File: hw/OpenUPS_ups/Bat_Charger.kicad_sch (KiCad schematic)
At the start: 63 parts, among them Q406 PMOS, Q601 2N7002, Q701 AON7534, U402 BD99950, U403 MCP6001R, U404 DZDH0401DW, U405 INA180A1, U801 NCP431

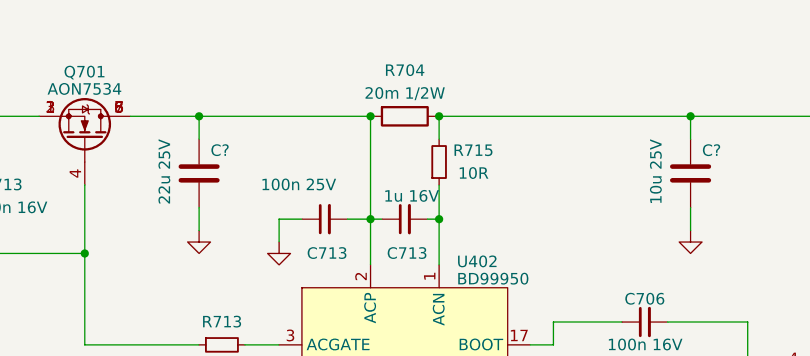
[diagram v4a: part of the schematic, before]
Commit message: Unified sense resistors to 10mR; Placement
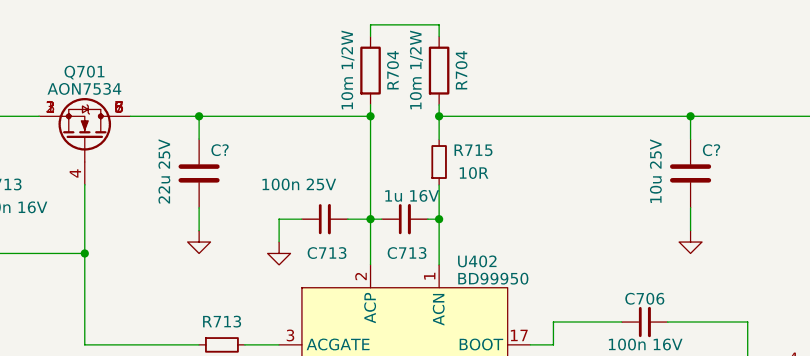
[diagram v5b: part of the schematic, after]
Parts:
- removed R704: 20m 1/2W, Resistor_SMD:R_2512_6332Metric, symbol Device:R
- added R704 (x2): 10m 1/2W, Resistor_SMD:R_1206_3216Metric, symbol Device:R
- R704: footprint Resistor_SMD:R_2512_6332Metric -> Resistor_SMD:R_1206_3216Metric
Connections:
- net at C?.1, Q701.5 (D), Q701.6 (D)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: now also R704.2
- net at C713.1, C713.2, C?.1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: now also R704.2
- new net: R704.1, R704.1
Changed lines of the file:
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@@
   (junction (at 186.69 78.74) (diameter 0) (color 0 0 0 0)
   )
-  (junction (at 161.29 25.4) (diameter 0) (color 0 0 0 0)
+  (junction (at 125.73 25.4) (diameter 0) (color 0 0 0 0)
   )
-  (junction (at 133.35 25.4) (diameter 0) (color 0 0 0 0)
+  (junction (at 161.29 25.4) (diameter 0) (color 0 0 0 0)
   )
   (junction (at 351.79 60.96) (diameter 0) (color 0 0 0 0)
@@
   (junction (at 245.11 69.85) (diameter 0) (color 0 0 0 0)
   )
-  (junction (at 125.73 25.4) (diameter 0) (color 0 0 0 0)
-  )
   (junction (at 133.35 36.83) (diameter 0) (color 0 0 0 0)
   )
@@
   (junction (at 240.03 217.17) (diameter 0) (color 0 0 0 0)
   )
+  (junction (at 133.35 25.4) (diameter 0) (color 0 0 0 0)
+  )
   (junction (at 368.3 102.87) (diameter 0) (color 0 0 0 0)
   )
@@
     (stroke (width 0) (type default))
   )
+  (wire (pts (xy 125.73 15.24) (xy 133.35 15.24))
+    (stroke (width 0) (type default))
+  )
   (wire (pts (xy 72.39 49.53) (xy 78.74 49.53))
     (stroke (width 0) (type default))
@@
     (stroke (width 0) (type default))
   )
-  (wire (pts (xy 133.35 25.4) (xy 161.29 25.4))
-    (stroke (width 0) (type default))
-  )
   (wire (pts (xy 80.01 36.83) (xy 80.01 40.64))
     (stroke (width 0) (type default))
@@
     (stroke (width 0) (type default))
   )
+  (wire (pts (xy 125.73 16.51) (xy 125.73 15.24))
+    (stroke (width 0) (type default))
+  )
   (wire (pts (xy 106.68 25.4) (xy 125.73 25.4))
     (stroke (width 0) (type default))
@@
     (stroke (width 0) (type default))
   )
+  (wire (pts (xy 133.35 25.4) (xy 133.35 24.13))
+    (stroke (width 0) (type default))
+  )
   (wire (pts (xy 106.68 38.1) (xy 106.68 35.56))
     (stroke (width 0) (type default))
@@
     (stroke (width 0) (type default))
   )
+  (wire (pts (xy 133.35 25.4) (xy 161.29 25.4))
+    (stroke (width 0) (type default))
+  )
   (wire (pts (xy 361.95 60.96) (xy 375.92 60.96))
     (stroke (width 0) (type default))
@@
     (stroke (width 0) (type default))
   )
+  (wire (pts (xy 125.73 24.13) (xy 125.73 25.4))
+    (stroke (width 0) (type default))
+  )
   (wire (pts (xy 361.95 73.66) (xy 361.95 71.12))
     (stroke (width 0) (type default))
@@
     (stroke (width 0) (type default))
   )
+  (wire (pts (xy 133.35 15.24) (xy 133.35 16.51))
+    (stroke (width 0) (type default))
+  )
   (wire (pts (xy 198.12 66.04) (xy 198.12 67.31))
     (stroke (width 0) (type default))
@@
     )
   )
+  (symbol (lib_id "Device:R") (at 125.73 20.32 0) (unit 1)
+    (in_bom yes) (on_board yes) (dnp no)
+    (property "Reference" "R704" (at 128.27 20.32 90)
+      (effects (font (size 1.27 1.27)))
+    )
+    (property "Value" "10m 1/2W" (at 123.19 20.32 90)
+      (effects (font (size 1.27 1.27)))
+    )
+    (property "Footprint" "Resistor_SMD:R_1206_3216Metric" (at 123.952 20.32 90)
+      (effects (font (size 1.27 1.27)) hide)
+    )
+    (property "Datasheet" "~" (at 125.73 20.32 0)
+      (effects (font (size 1.27 1.27)) hide)
+    )
+    (pin "1")
+    (pin "2")
+    (instances
+      (project "OpenUPS_ups"
+        (path "/f77faec3-eac4-47f3-a2de-ec4a039f4502/09fcd86a-cc7e-4bce-97cb-42a94055ba63"
+          (reference "R704") (unit 1)
+        )
+        (path "/f77faec3-eac4-47f3-a2de-ec4a039f4502/dfbaaed0-e564-4e21-900d-d5a65c0f1694"
+          (reference "R410") (unit 1)
+        )
+        (path "/f77faec3-eac4-47f3-a2de-ec4a039f4502/0bd99307-a15c-41e8-997b-077d576f806c"
+          (reference "R424") (unit 1)
+        )
+      )
+    )
+  )
   (symbol (lib_id "power:GND") (at 281.94 77.47 90) (unit 1)
     (in_bom yes) (on_board yes) (dnp no)
@@
     )
   )
+  (symbol (lib_id "Device:R") (at 133.35 20.32 0) (unit 1)
+    (in_bom yes) (on_board yes) (dnp no)
+    (property "Reference" "R704" (at 135.89 20.32 90)
+      (effects (font (size 1.27 1.27)))
+    )
+    (property "Value" "10m 1/2W" (at 130.81 20.32 90)
+      (effects (font (size 1.27 1.27)))
+    )
+    (property "Footprint" "Resistor_SMD:R_1206_3216Metric" (at 131.572 20.32 90)
+      (effects (font (size 1.27 1.27)) hide)
+    )
+    (property "Datasheet" "~" (at 133.35 20.32 0)
+      (effects (font (size 1.27 1.27)) hide)
+    )
+    (pin "1")
+    (pin "2")
+    (instances
+      (project "OpenUPS_ups"
+        (path "/f77faec3-eac4-47f3-a2de-ec4a039f4502/09fcd86a-cc7e-4bce-97cb-42a94055ba63"
+          (reference "R704") (unit 1)
+        )
+        (path "/f77faec3-eac4-47f3-a2de-ec4a039f4502/dfbaaed0-e564-4e21-900d-d5a65c0f1694"
+          (reference "R410") (unit 1)
+        )
+        (path "/f77faec3-eac4-47f3-a2de-ec4a039f4502/0bd99307-a15c-41e8-997b-077d576f806c"
+          (reference "R409") (unit 1)
+        )
+      )
+    )
+  )
   (symbol (lib_id "Amplifier_Operational:MCP6001R") (at 252.73 217.17 0) (mirror y) (unit 1)
     (in_bom yes) (on_board yes) (dnp no)
@@
       (effects (font (size 1.27 1.27)))
     )
-    (property "Footprint" "Resistor_SMD:R_2512_6332Metric" (at 220.218 83.82 90)
+    (property "Footprint" "Resistor_SMD:R_1206_3216Metric" (at 220.218 83.82 90)
       (effects (font (size 1.27 1.27)) hide)
     )
@@
       (effects (font (size 1.27 1.27)))
     )
-    (property "Footprint" "Resistor_SMD:R_2512_6332Metric" (at 229.108 83.82 90)
+    (property "Footprint" "Resistor_SMD:R_1206_3216Metric" (at 229.108 83.82 90)
       (effects (font (size 1.27 1.27)) hide)
     )
@@
         )
       )
-    )
-  )
-  (symbol (lib_id "Device:R") (at 129.54 25.4 270) (unit 1)
-    (in_bom yes) (on_board yes) (dnp no)
-    (property "Reference" "R704" (at 129.54 20.32 90)
-      (effects (font (size 1.27 1.27)))
-    )
-    (property "Value" "20m 1/2W" (at 129.54 22.86 90)
-      (effects (font (size 1.27 1.27)))
-    )
-    (property "Footprint" "Resistor_SMD:R_2512_6332Metric" (at 129.54 23.622 90)
-      (effects (font (size 1.27 1.27)) hide)
-    )
-    (property "Datasheet" "~" (at 129.54 25.4 0)
-      (effects (font (size 1.27 1.27)) hide)
-    )
-    (pin "1")
-    (pin "2")
-    (instances
-      (project "OpenUPS_ups"
-        (path "/f77faec3-eac4-47f3-a2de-ec4a039f4502/09fcd86a-cc7e-4bce-97cb-42a94055ba63"
-          (reference "R704") (unit 1)
-        )
-        (path "/f77faec3-eac4-47f3-a2de-ec4a039f4502/dfbaaed0-e564-4e21-900d-d5a65c0f1694"
-          (reference "R410") (unit 1)
-        )
-        (path "/f77faec3-eac4-47f3-a2de-ec4a039f4502/0bd99307-a15c-41e8-997b-077d576f806c"
-          (reference "R409") (unit 1)
-        )
-      )

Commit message: Layout WIP
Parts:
- removed R704: 10m 1/2W, Resistor_SMD:R_1206_3216Metric, symbol Device:R
- Q406: value PMOS -> AON7423; footprint (none) -> footprints:DFN 3x3 MOSFET
- R704: value 10m 1/2W -> 20m 1/2W
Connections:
- net +BATT: now also Q406.5 (D), Q406.6 (D), Q406.7 (D), Q406.8 (D); no longer Q406.1 (D)
- net Vsys: now also Q406.1 (S), Q406.2 (S)
- net at C?.1, Q701.5 (D), Q701.6 (D)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: now also R704.1
- net at R305.1, R305.2, U404.3 (BIAS): now also Q406.4 (G); no longer Q406.2 (G)
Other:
- moved on the sheet: R704
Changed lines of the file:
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@@
   (junction (at 186.69 78.74) (diameter 0) (color 0 0 0 0)
   )
+  (junction (at 161.29 25.4) (diameter 0) (color 0 0 0 0)
+  )
+  (junction (at 351.79 60.96) (diameter 0) (color 0 0 0 0)
+  )
+  (junction (at 300.99 60.96) (diameter 0) (color 0 0 0 0)
+  )
+  (junction (at 67.31 25.4) (diameter 0) (color 0 0 0 0)
+  )
+  (junction (at 198.12 60.96) (diameter 0) (color 0 0 0 0)
+  )
+  (junction (at 321.31 60.96) (diameter 0) (color 0 0 0 0)
+  )
+  (junction (at 167.64 60.96) (diameter 0) (color 0 0 0 0)
+  )
+  (junction (at 57.15 25.4) (diameter 0) (color 0 0 0 0)
+  )
+  (junction (at 87.63 100.33) (diameter 0) (color 0 0 0 0)
+  )
+  (junction (at 245.11 60.96) (diameter 0) (color 0 0 0 0)
+  )
+  (junction (at 179.07 60.96) (diameter 0) (color 0 0 0 0)
+  )
+  (junction (at 255.27 207.01) (diameter 0) (color 0 0 0 0)
+  )
+  (junction (at 153.67 86.36) (diameter 0) (color 0 0 0 0)
+  )
+  (junction (at 245.11 69.85) (diameter 0) (color 0 0 0 0)
+  )
+  (junction (at 133.35 36.83) (diameter 0) (color 0 0 0 0)
+  )
+  (junction (at 96.52 110.49) (diameter 0) (color 0 0 0 0)
+  )
+  (junction (at 245.11 87.63) (diameter 0) (color 0 0 0 0)
+  )
+  (junction (at 96.52 102.87) (diameter 0) (color 0 0 0 0)
+  )
+  (junction (at 361.95 60.96) (diameter 0) (color 0 0 0 0)
+  )
+  (junction (at 80.01 25.4) (diameter 0) (color 0 0 0 0)
+  )
+  (junction (at 255.27 69.85) (diameter 0) (color 0 0 0 0)
+  )
+  (junction (at 48.26 66.04) (diameter 0) (color 0 0 0 0)
+  )
+  (junction (at 240.03 217.17) (diameter 0) (color 0 0 0 0)
+  )
+  (junction (at 368.3 102.87) (diameter 0) (color 0 0 0 0)
+  )
+  (junction (at 218.44 60.96) (diameter 0) (color 0 0 0 0)
+  )
   (junction (at 125.73 25.4) (diameter 0) (color 0 0 0 0)
   )
-  (junction (at 161.29 25.4) (diameter 0) (color 0 0 0 0)
-  )
-  (junction (at 351.79 60.96) (diameter 0) (color 0 0 0 0)
-  )
-  (junction (at 300.99 60.96) (diameter 0) (color 0 0 0 0)
-  )
-  (junction (at 67.31 25.4) (diameter 0) (color 0 0 0 0)
-  )
-  (junction (at 198.12 60.96) (diameter 0) (color 0 0 0 0)
-  )
-  (junction (at 321.31 60.96) (diameter 0) (color 0 0 0 0)
-  )
-  (junction (at 167.64 60.96) (diameter 0) (color 0 0 0 0)
-  )
-  (junction (at 57.15 25.4) (diameter 0) (color 0 0 0 0)
-  )
-  (junction (at 87.63 100.33) (diameter 0) (color 0 0 0 0)
-  )
-  (junction (at 245.11 60.96) (diameter 0) (color 0 0 0 0)
-  )
-  (junction (at 179.07 60.96) (diameter 0) (color 0 0 0 0)
-  )
-  (junction (at 255.27 207.01) (diameter 0) (color 0 0 0 0)
-  )
-  (junction (at 153.67 86.36) (diameter 0) (color 0 0 0 0)
-  )
-  (junction (at 245.11 69.85) (diameter 0) (color 0 0 0 0)
-  )
-  (junction (at 133.35 36.83) (diameter 0) (color 0 0 0 0)
-  )
-  (junction (at 96.52 110.49) (diameter 0) (color 0 0 0 0)
-  )
-  (junction (at 245.11 87.63) (diameter 0) (color 0 0 0 0)
-  )
-  (junction (at 96.52 102.87) (diameter 0) (color 0 0 0 0)
-  )
-  (junction (at 361.95 60.96) (diameter 0) (color 0 0 0 0)
-  )
-  (junction (at 80.01 25.4) (diameter 0) (color 0 0 0 0)
-  )
-  (junction (at 255.27 69.85) (diameter 0) (color 0 0 0 0)
-  )
-  (junction (at 48.26 66.04) (diameter 0) (color 0 0 0 0)
-  )
-  (junction (at 240.03 217.17) (diameter 0) (color 0 0 0 0)
+  (junction (at 245.11 77.47) (diameter 0) (color 0 0 0 0)
+  )
+  (junction (at 218.44 88.9) (diameter 0) (color 0 0 0 0)
+  )
+  (junction (at 273.05 77.47) (diameter 0) (color 0 0 0 0)
+  )
+  (junction (at 125.73 36.83) (diameter 0) (color 0 0 0 0)
+  )
+  (junction (at 311.15 60.96) (diameter 0) (color 0 0 0 0)
   )
   (junction (at 133.35 25.4) (diameter 0) (color 0 0 0 0)
   )
-  (junction (at 368.3 102.87) (diameter 0) (color 0 0 0 0)
-  )
-  (junction (at 218.44 60.96) (diameter 0) (color 0 0 0 0)
-  )
-  (junction (at 245.11 77.47) (diameter 0) (color 0 0 0 0)
-  )
-  (junction (at 218.44 88.9) (diameter 0) (color 0 0 0 0)
-  )
-  (junction (at 273.05 77.47) (diameter 0) (color 0 0 0 0)
-  )
-  (junction (at 125.73 36.83) (diameter 0) (color 0 0 0 0)
-  )
-  (junction (at 311.15 60.96) (diameter 0) (color 0 0 0 0)
-  )
   (junction (at 341.63 60.96) (diameter 0) (color 0 0 0 0)
   )
@@
     (stroke (width 0) (type default))
   )
-  (wire (pts (xy 125.73 15.24) (xy 133.35 15.24))
-    (stroke (width 0) (type default))
-  )
   (wire (pts (xy 72.39 49.53) (xy 78.74 49.53))
     (stroke (width 0) (type default))
@@
     (stroke (width 0) (type default))
   )
-  (wire (pts (xy 125.73 16.51) (xy 125.73 15.24))
-    (stroke (width 0) (type default))
-  )
   (wire (pts (xy 106.68 25.4) (xy 125.73 25.4))
     (stroke (width 0) (type default))
@@
     (stroke (width 0) (type default))
   )
-  (wire (pts (xy 133.35 25.4) (xy 133.35 24.13))
-    (stroke (width 0) (type default))
-  )
   (wire (pts (xy 106.68 38.1) (xy 106.68 35.56))
     (stroke (width 0) (type default))
@@
     (stroke (width 0) (type default))
   )
-  (wire (pts (xy 125.73 24.13) (xy 125.73 25.4))
-    (stroke (width 0) (type default))
-  )
   (wire (pts (xy 361.95 73.66) (xy 361.95 71.12))
     (stroke (width 0) (type default))
@@
   )
   (wire (pts (xy 80.01 25.4) (xy 80.01 31.75))
-    (stroke (width 0) (type default))
-  )
-  (wire (pts (xy 133.35 15.24) (xy 133.35 16.51))
     (stroke (width 0) (type default))
   )
@@
   )
   (symbol (lib_id "Simulation_SPICE:PMOS") (at 247.65 82.55 180) (unit 1)
-    (in_bom yes) (on_board yes) (dnp no) (fields_autoplaced)
-    (property "Reference" "Q406" (at 240.1951 82.55 90)
-      (effects (font (size 1.27 1.27)))
-    )
-    (property "Value" "PMOS" (at 242.1161 82.55 90)
-      (effects (font (size 1.27 1.27)))
-    )
-    (property "Footprint" "" (at 242.57 85.09 0)
-      (effects (font (size 1.27 1.27)) hide)
-    )
-    (property "Datasheet" "https://ngspice.sourceforge.io/docs/ngspice-manual.pdf" (at 247.65 69.85 0)
-      (effects (font (size 1.27 1.27)) hide)
-    )
-    (property "Sim.Device" "PMOS" (at 247.65 65.405 0)
-      (effects (font (size 1.27 1.27)) hide)
-    )
-    (property "Sim.Type" "VDMOS" (at 247.65 63.5 0)
-      (effects (font (size 1.27 1.27)) hide)
-    )
-    (property "Sim.Pins" "1=D 2=G 3=S" (at 247.65 67.31 0)
-      (effects (font (size 1.27 1.27)) hide)
-    )
-    (pin "1")
-    (pin "2")
+    (in_bom yes) (on_board yes) (dnp no)
+    (property "Reference" "Q406" (at 238.76 82.55 90)
+      (effects (font (size 1.27 1.27)))
+    )
+    (property "Value" "AON7423" (at 241.3 82.55 90)
+      (effects (font (size 1.27 1.27)))
+    )
+    (property "Footprint" "footprints:DFN 3x3 MOSFET" (at 252.73 80.01 0)
+      (effects (font (size 1.27 1.27)) hide)
+    )
+    (property "Datasheet" "https://www.tme.eu/Document/f617947f937affdcef3d2ac1a885827c/AON7423-DTE.pdf" (at 247.65 95.25 0)
+      (effects (font (size 1.27 1.27)) hide)
+    )
+    (pin "5")
+    (pin "6")
+    (pin "7")
+    (pin "8")
+    (pin "1")
     (pin "3")
+    (pin "2")
+    (pin "4")
     (instances
       (project "OpenUPS_ups"
@@
     )
   )
-  (symbol (lib_id "Device:R") (at 125.73 20.32 0) (unit 1)
-    (in_bom yes) (on_board yes) (dnp no)
-    (property "Reference" "R704" (at 128.27 20.32 90)
-      (effects (font (size 1.27 1.27)))
-    )
-    (property "Value" "10m 1/2W" (at 123.19 20.32 90)
-      (effects (font (size 1.27 1.27)))
-    )
-    (property "Footprint" "Resistor_SMD:R_1206_3216Metric" (at 123.952 20.32 90)
-      (effects (font (size 1.27 1.27)) hide)
-    )
-    (property "Datasheet" "~" (at 125.73 20.32 0)
+  (symbol (lib_id "Device:R") (at 129.54 25.4 270) (unit 1)
+    (in_bom yes) (on_board yes) (dnp no)
+    (property "Reference" "R704" (at 129.54 27.94 90)
+      (effects (font (size 1.27 1.27)))
+    )
+    (property "Value" "20m 1/2W" (at 129.54 22.86 90)
+      (effects (font (size 1.27 1.27)))
+    )
+    (property "Footprint" "Resistor_SMD:R_1206_3216Metric" (at 129.54 23.622 90)
+      (effects (font (size 1.27 1.27)) hide)
+    )
+    (property "Datasheet" "~" (at 129.54 25.4 0)
       (effects (font (size 1.27 1.27)) hide)
     )
@@
         )
       )
-    )
-  )
-  (symbol (lib_id "Device:R") (at 133.35 20.32 0) (unit 1)
-    (in_bom yes) (on_board yes) (dnp no)
-    (property "Reference" "R704" (at 135.89 20.32 90)
-      (effects (font (size 1.27 1.27)))
-    )
-    (property "Value" "10m 1/2W" (at 130.81 20.32 90)
-      (effects (font (size 1.27 1.27)))
-    )
-    (property "Footprint" "Resistor_SMD:R_1206_3216Metric" (at 131.572 20.32 90)
-      (effects (font (size 1.27 1.27)) hide)
-    )
-    (property "Datasheet" "~" (at 133.35 20.32 0)
-      (effects (font (size 1.27 1.27)) hide)
-    )
-    (pin "1")
-    (pin "2")
-    (instances
-      (project "OpenUPS_ups"
-        (path "/f77faec3-eac4-47f3-a2de-ec4a039f4502/09fcd86a-cc7e-4bce-97cb-42a94055ba63"
-          (reference "R704") (unit 1)
-        )
-        (path "/f77faec3-eac4-47f3-a2de-ec4a039f4502/dfbaaed0-e564-4e21-900d-d5a65c0f1694"
-          (reference "R410") (unit 1)
-        )
-        (path "/f77faec3-eac4-47f3-a2de-ec4a039f4502/0bd99307-a15c-41e8-997b-077d576f806c"
-          (reference "R409") (unit 1)
-        )
-      )

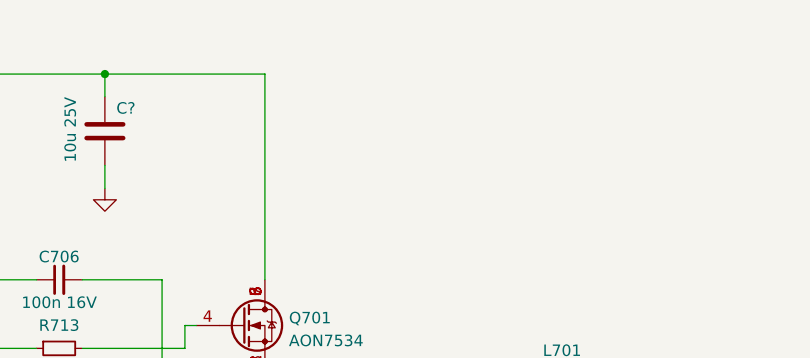
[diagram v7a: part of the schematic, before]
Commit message: Introducing reverse polarity protected adapter voltage
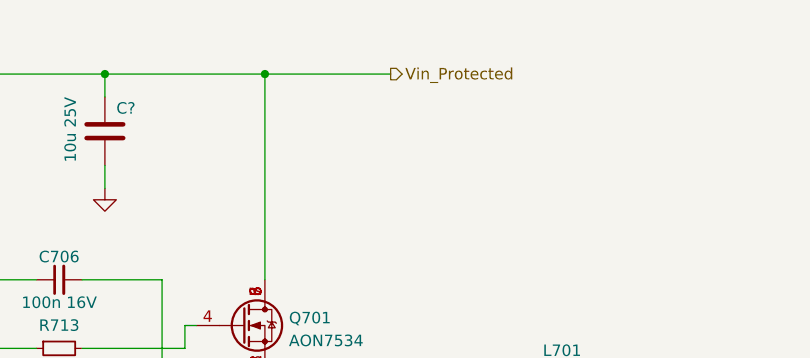
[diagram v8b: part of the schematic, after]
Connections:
- net Vin_Protected: now reaches C?.1, Q701.5 (D), Q701.6 (D), Q701.7 (D), Q701.8 (D), R704.1, R715.2
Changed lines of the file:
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@@
   (junction (at 361.95 60.96) (diameter 0) (color 0 0 0 0)
   )
+  (junction (at 179.07 25.4) (diameter 0) (color 0 0 0 0)
+  )
   (junction (at 80.01 25.4) (diameter 0) (color 0 0 0 0)
   )
@@
   )
   (wire (pts (xy 125.73 36.83) (xy 125.73 41.91))
+    (stroke (width 0) (type default))
+  )
+  (wire (pts (xy 179.07 25.4) (xy 193.04 25.4))
     (stroke (width 0) (type default))
   )
@@
     (effects (font (size 1.27 1.27)) (justify right))
   )
+  (hierarchical_label "Vin_Protected" (shape output) (at 193.04 25.4 0) (fields_autoplaced)
+    (effects (font (size 1.27 1.27)) (justify left))
+  )
   (symbol (lib_id "Device:C_Small") (at 109.22 66.04 90) (unit 1)
